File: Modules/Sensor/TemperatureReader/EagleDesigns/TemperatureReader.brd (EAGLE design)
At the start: 100 x 80 mm, 11 parts, among them U1 MLX90614, U2 ATMEGA328P_TQFP

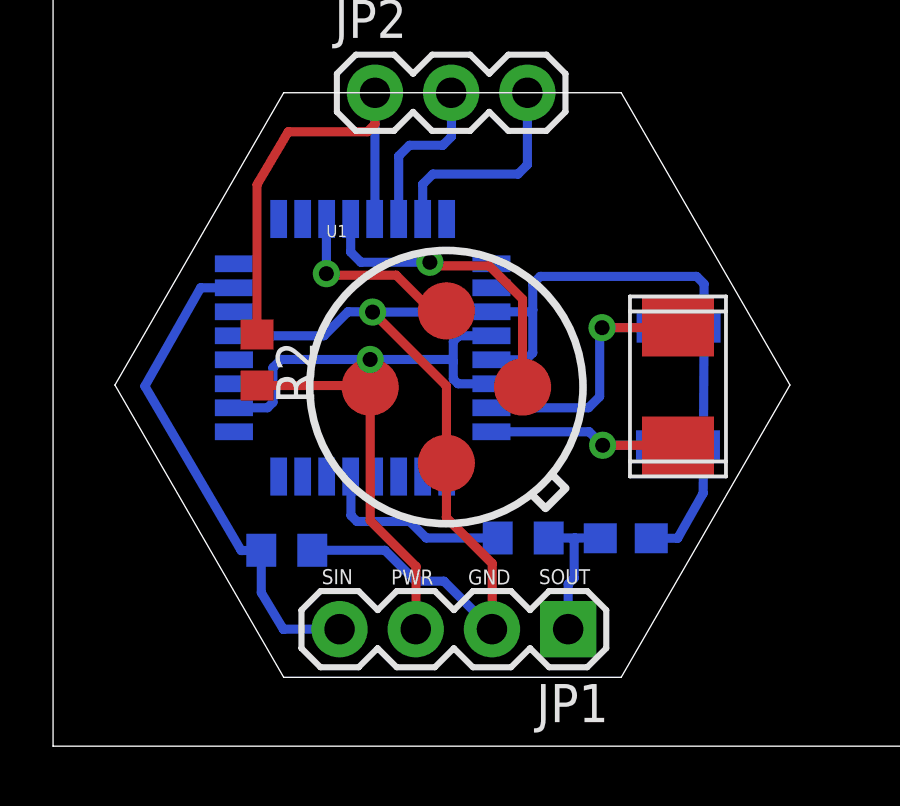
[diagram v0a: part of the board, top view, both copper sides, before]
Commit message: changed visible layers
just for designing. this made it easier to design the multi-layer PCB
with every other layer set to be invisible.
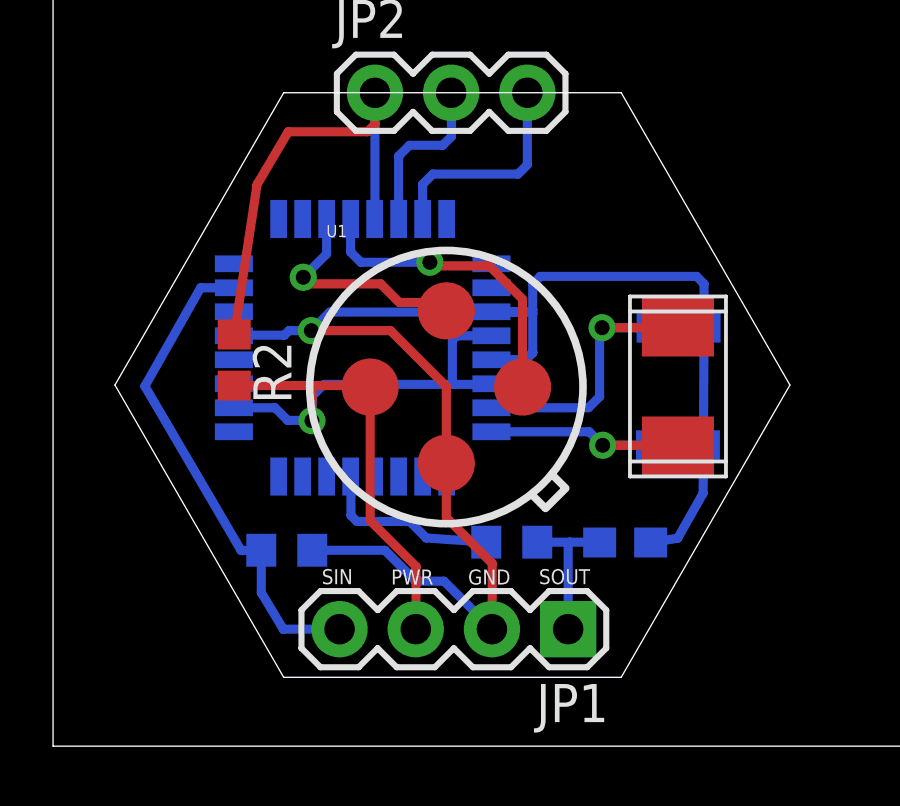
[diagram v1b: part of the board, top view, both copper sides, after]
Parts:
- moved R2 0.76 mm to (6.04, 12.9)
- moved R4 0.40 mm to (15.3, 6.80)
- moved C3 0.14 mm to (19.1, 6.79)
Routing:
- net GND: track 48.9 -> 53.6 mm
- net SDA: track 6.34 -> 7.56 mm
- net VCC: track 26.1 -> 27.0 mm

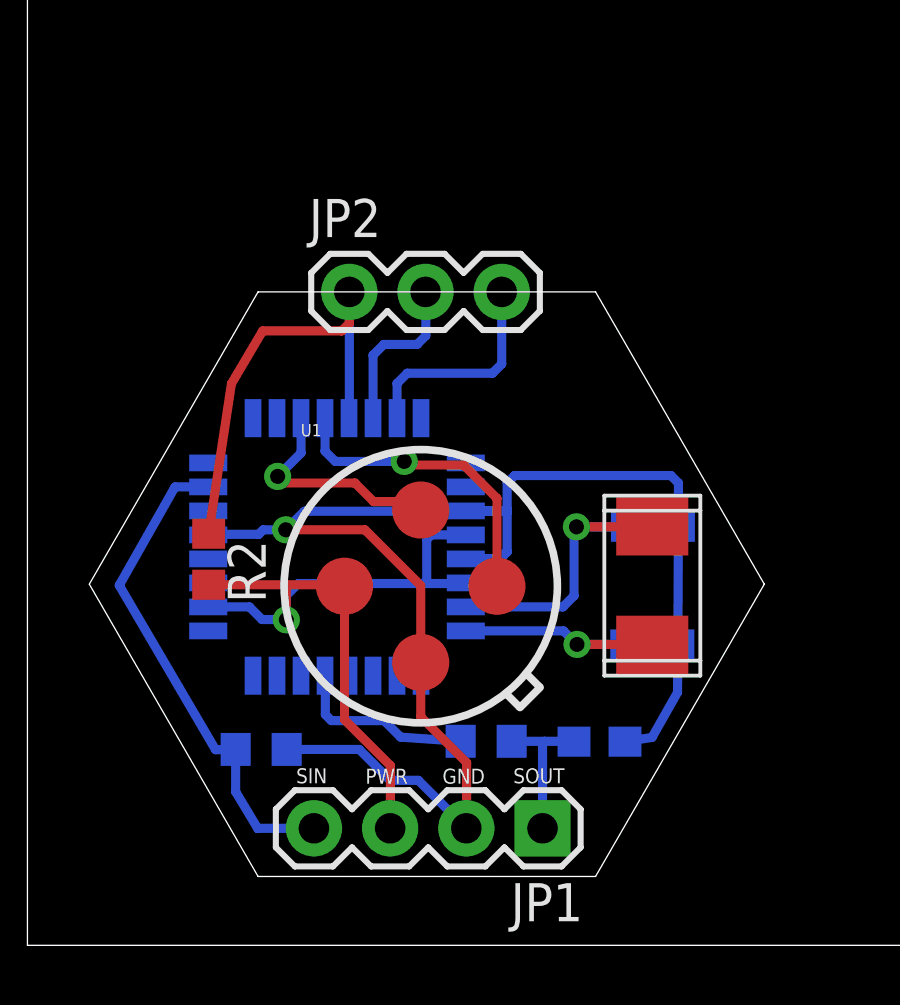
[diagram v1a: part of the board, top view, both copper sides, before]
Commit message: added version numbers, and deleted most of the text that was on each module.
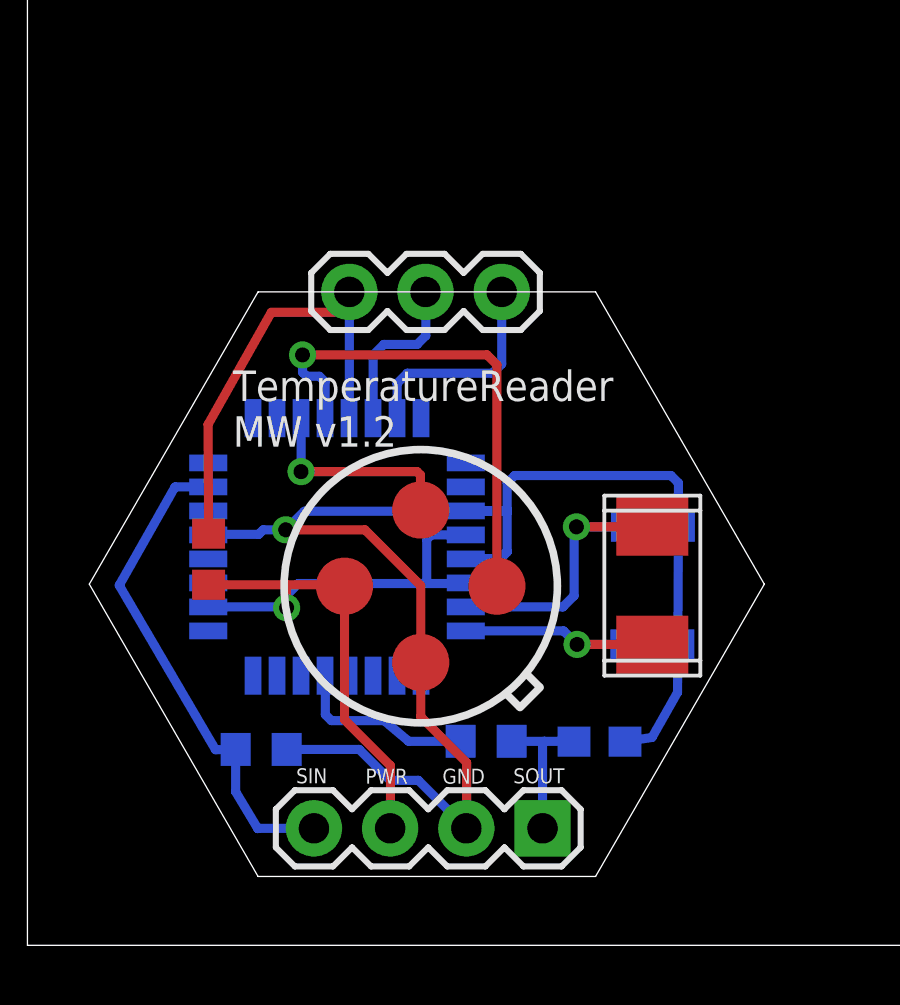
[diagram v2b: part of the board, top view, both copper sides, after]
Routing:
- net SCL: track 10.4 -> 16.7 mm
- net VCC: track 27.0 -> 26.1 mm
- net SDA: track 7.56 -> 6.98 mm
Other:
- board text added: "TemperatureReader MW v1.2"

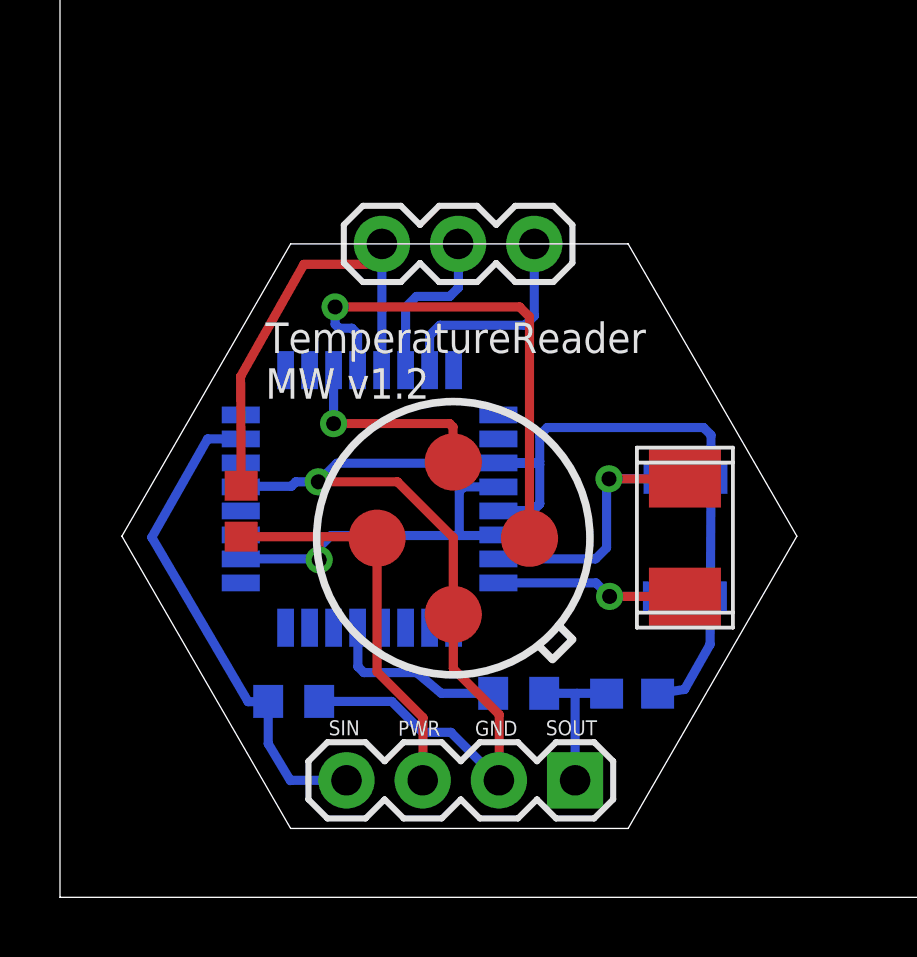
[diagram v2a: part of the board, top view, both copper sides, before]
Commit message: TemperatureReader: removed crystal, modified to work with new bootloader #31
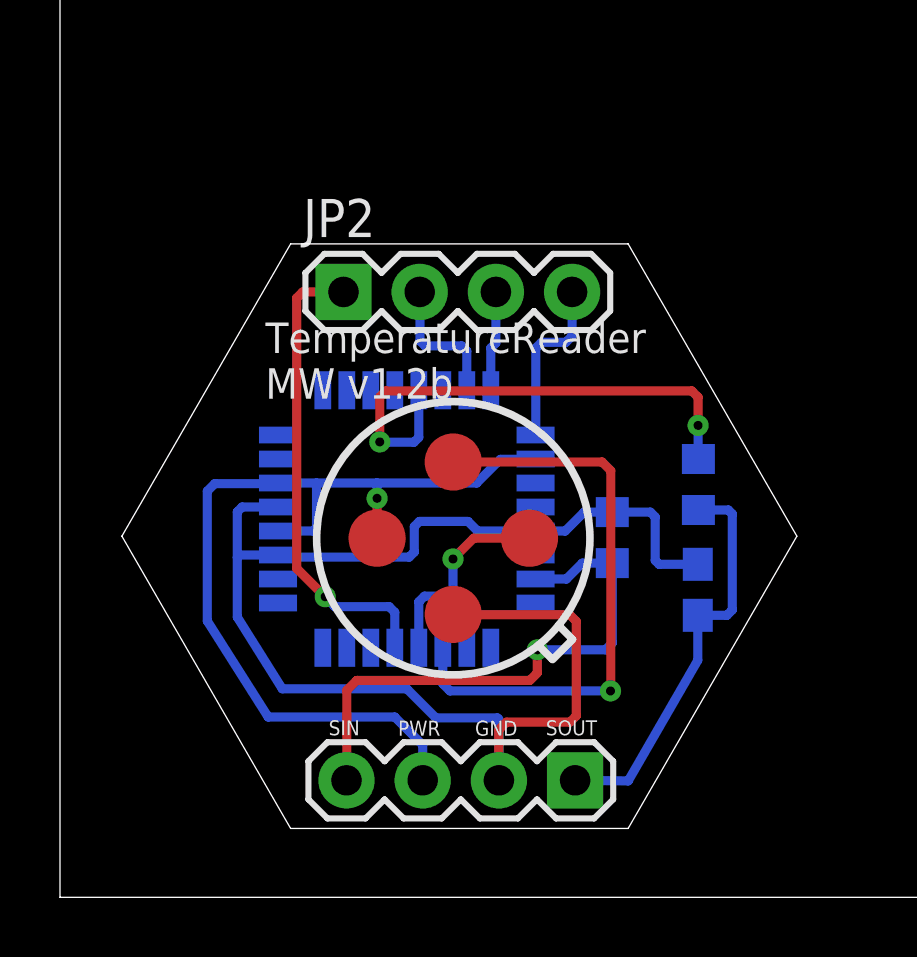
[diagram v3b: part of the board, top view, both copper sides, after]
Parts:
- removed C1, C2: 22pF, adafruit:C0603
- removed R2: 10K, resistor:R0603
- removed U$2: NX503, MakerWear:NX503
- JP2: device SparkFun-Connectors:1X03 -> SparkFun-Connectors:1X04
- moved R1 11.9 mm to (18.4, 12.0), turned to 270 degrees
- moved R4 9.18 mm to (21.3, 13.8), turned to 90 degrees
- moved C3 4.09 mm to (21.3, 10.2), turned to 90 degrees
- moved JP2 2.05 mm to (9.45, 20.2)
- moved U2 1.41 mm to (11.6, 12.6), turned to 180 degrees
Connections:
- removed net N$1: C1.1, U$2.P$1, U2.7
- removed net N$3: C2.1, U$2.P$2, U2.8
- removed net RX: JP2.2, U2.30
- removed net TX: JP2.3, U2.31
- new net MISO: JP2.3, U2.16
- new net MOSI: JP2.2, U2.15
- new net SCK: JP2.4, U2.17
- net GND: no longer C1.2, C2.2
- net RESET: no longer R2.1
- net VCC: no longer R2.2
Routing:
- net SDA: track 6.98 -> 19.6 mm
- net OUT: track 6.15 -> 17.3 mm, vias 0 -> 2
- net N$1: track 10.3 -> 0.00 mm, vias 1 -> 0
- net SCL: track 16.7 -> 6.74 mm
- net 1X3SOUT: track 5.01 -> 13.5 mm
- net N$3: track 8.08 -> 0.00 mm, vias 1 -> 0
- net TX: track 7.32 -> 0.00 mm
- net GND: track 53.6 -> 47.6 mm, vias 1 -> 0
- net SCK: track 0.00 -> 5.75 mm
- net RX: track 5.59 -> 0.00 mm
- net VCC: track 26.1 -> 30.9 mm
- net MOSI: track 0.00 -> 4.64 mm
- net MISO: track 0.00 -> 3.35 mm
- net 1X3SIN: track 16.6 -> 18.4 mm, vias 0 -> 1
- net RESET: track 15.5 -> 15.7 mm, vias 0 -> 1
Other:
- board text added: "TemperatureReader MW v1.2b"
- board text removed: "TemperatureReader MW v1.2"
